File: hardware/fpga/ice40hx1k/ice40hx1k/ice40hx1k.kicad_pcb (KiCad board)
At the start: 2 copper layers, 58 parts, among them J1 Conn_01x20_Male, J2 Conn_01x20_Male, J3 Conn_01x20_Male, U1 LTC3406ES5, U5 AT25SF081-SSHD-X, U6 ICE40HX1K-VQ100(VQFP100), U7 AS7C34096A, X2 ASE-10MHz, X3 ASE-10MHz, X4 ASE-10MHz, X5 ASV-xxxMHz, X6 ASV-xxxMHz, X7 ASV-xxxMHz

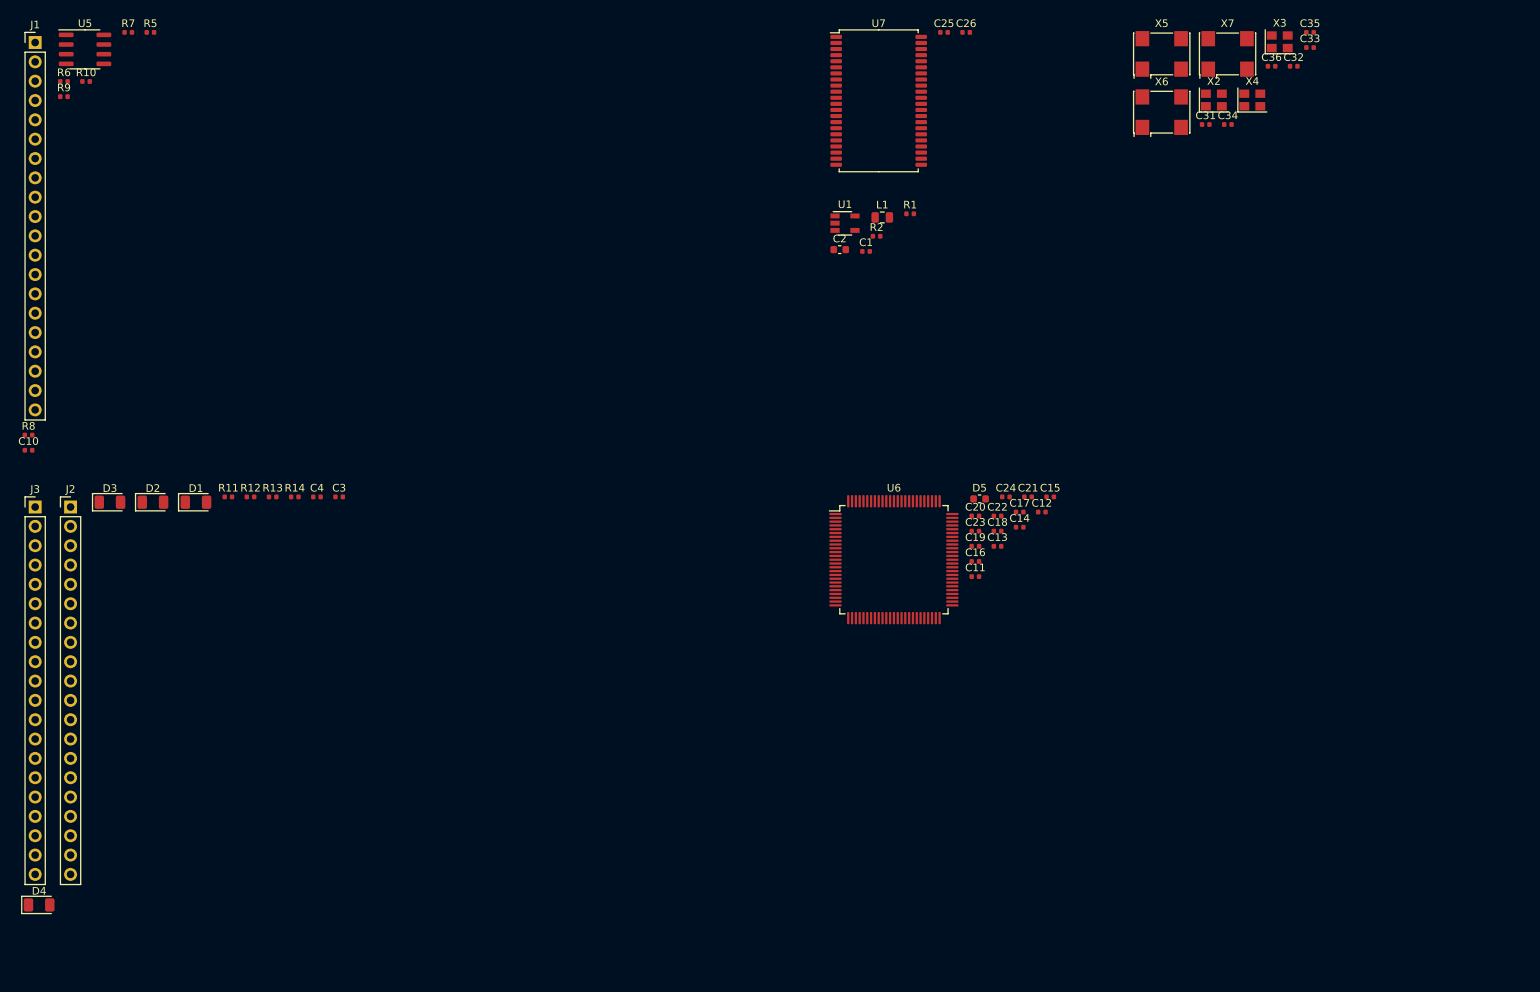
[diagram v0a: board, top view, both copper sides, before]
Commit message: std FPGA skeleton
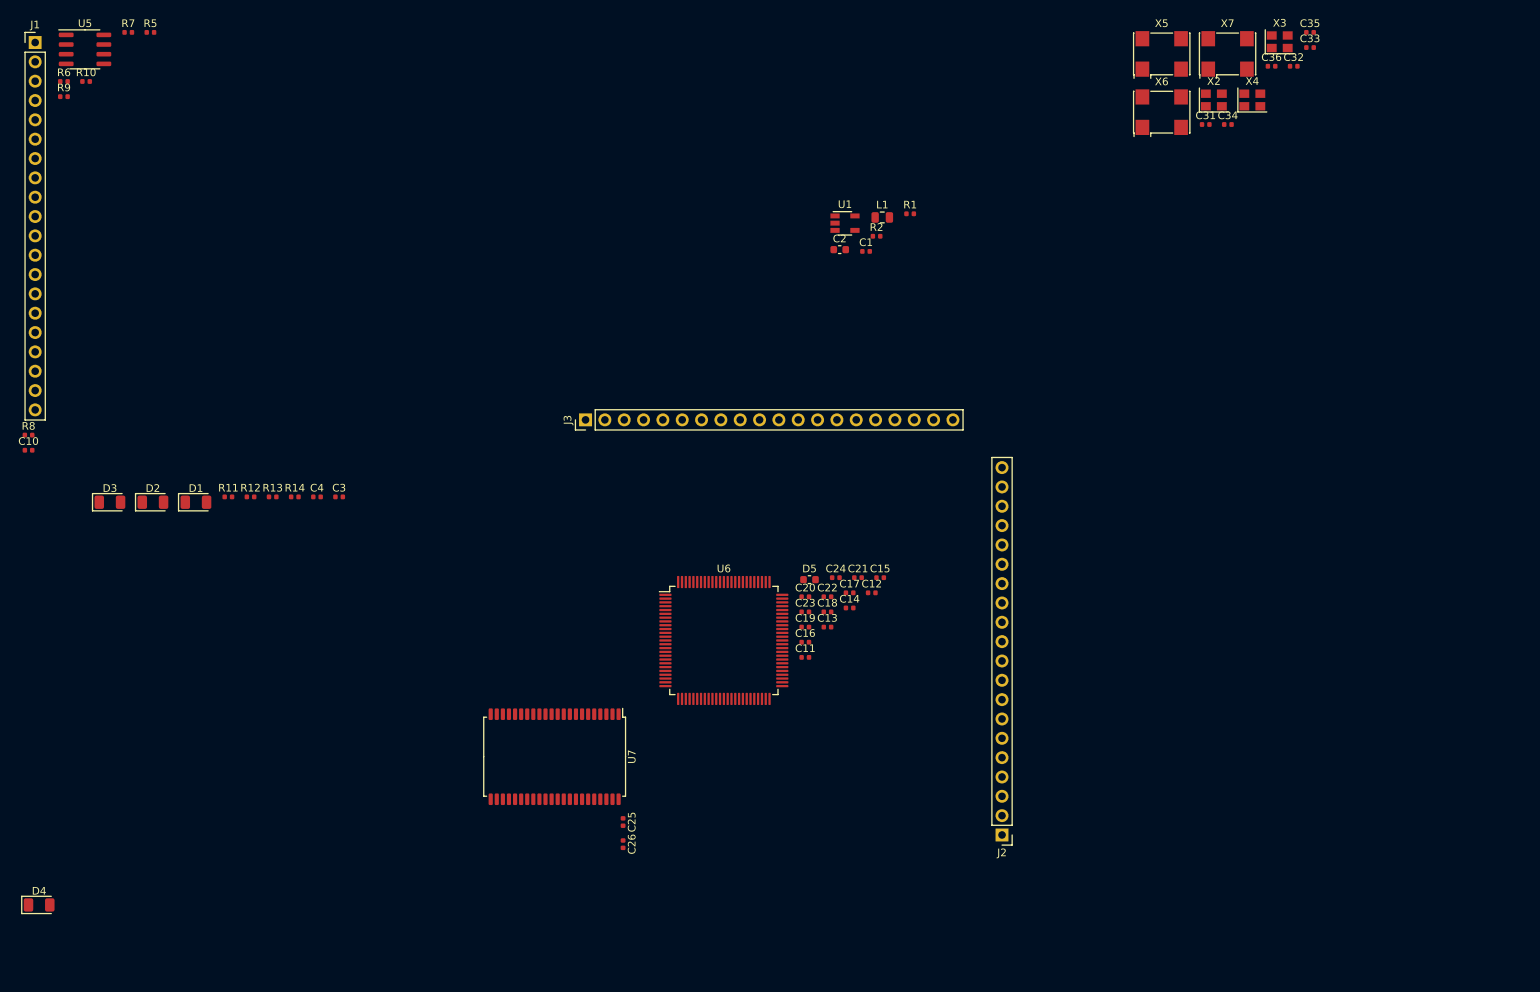
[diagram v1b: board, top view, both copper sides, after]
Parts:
- moved J2 129.7 mm to (191.9, 145.3), turned to 180 degrees
- moved C26 115.8 mm to (142.1, 146.5), turned to 270 degrees
- moved C25 112.0 mm to (142.1, 143.6), turned to 270 degrees
- moved U7 96.1 mm to (133.1, 135.0), turned to 270 degrees
- moved J3 73.2 mm to (137.2, 90.7), turned to 90 degrees
- moved C11 24.7 mm to (166.0, 121.9)
- moved C12 24.7 mm to (174.8, 113.5)
- moved C13 24.7 mm to (168.9, 118.0)
- moved C15 24.7 mm to (175.9, 111.5)
- moved C16 24.7 mm to (166.0, 120.0)
- moved C18 24.7 mm to (168.9, 116.0)
- moved C19 24.7 mm to (166.0, 118.0)
- moved C20 24.7 mm to (166.0, 114.0)
- moved C21 24.7 mm to (173.0, 111.5)
- moved C22 24.7 mm to (168.9, 114.0)
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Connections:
- J2 pad 12: IO100 -> IO78
- J2 pad 14: IO99 -> IO79
- J2 pad 16: IO97 -> IO80
- J2 pad 17: IO96 -> IO81
- J2 pad 18: IO95 -> IO82
- J2 pad 19: IO94 -> IO83
- J3 pad 11: IO85 -> IO93
- J3 pad 12: IO83 -> IO91
- J3 pad 14: IO82 -> IO90
- J3 pad 16: IO81 -> IO89
- J3 pad 17: IO80 -> IO87
- J3 pad 18: IO79 -> IO86
- J3 pad 19: IO78 -> IO85
- J3 pad 2: IO93 -> IO100
- J3 pad 3: IO91 -> IO99
- J3 pad 5: IO90 -> IO97
- J3 pad 6: IO89 -> IO96
- J3 pad 8: IO87 -> IO95
- J3 pad 9: IO86 -> IO94

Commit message: std FPGA skeleton
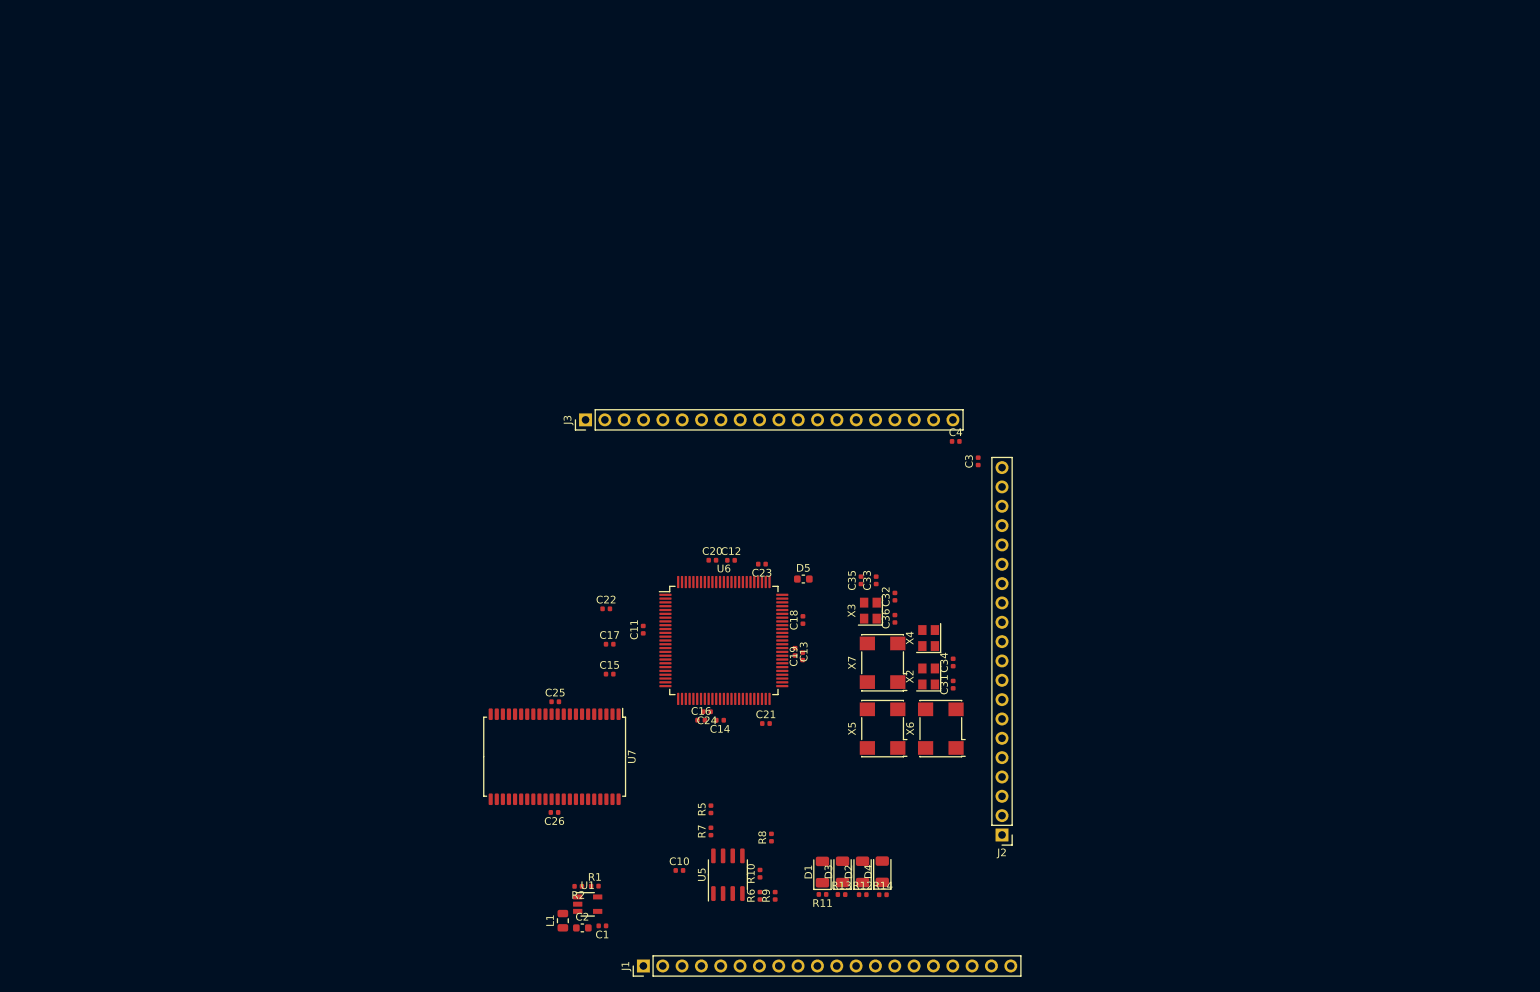
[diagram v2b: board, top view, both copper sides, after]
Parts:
- moved J1 145.3 mm to (144.8, 162.5), turned to 90 degrees
- moved R6 140.7 mm to (160.1, 153.3), turned to 90 degrees
- moved R9 140.5 mm to (162.1, 153.3), turned to 90 degrees
- moved U5 137.4 mm to (155.9, 150.5), turned to 90 degrees
- moved R10 136.6 mm to (160.1, 150.3), turned to 90 degrees
- moved R7 129.9 mm to (153.6, 144.8), turned to 90 degrees
- moved R5 125.8 mm to (153.6, 141.9), turned to 90 degrees
- moved R8 111.0 mm to (161.6, 145.6), turned to 90 degrees
- moved D4 110.8 mm to (176.2, 150.1), turned to 90 degrees
- moved D3 107.8 mm to (170.9, 150.1), turned to 90 degrees
- moved D2 105.1 mm to (173.6, 150.1), turned to 90 degrees
- moved C10 101.8 mm to (149.5, 149.9)
- moved L1 101.5 mm to (134.2, 156.5), turned to 90 degrees
- moved R1 97.6 mm to (138.4, 152.0)
- moved X5 95.9 mm to (176.2, 131.3), turned to 90 degrees
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
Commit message: std FPGA skeleton
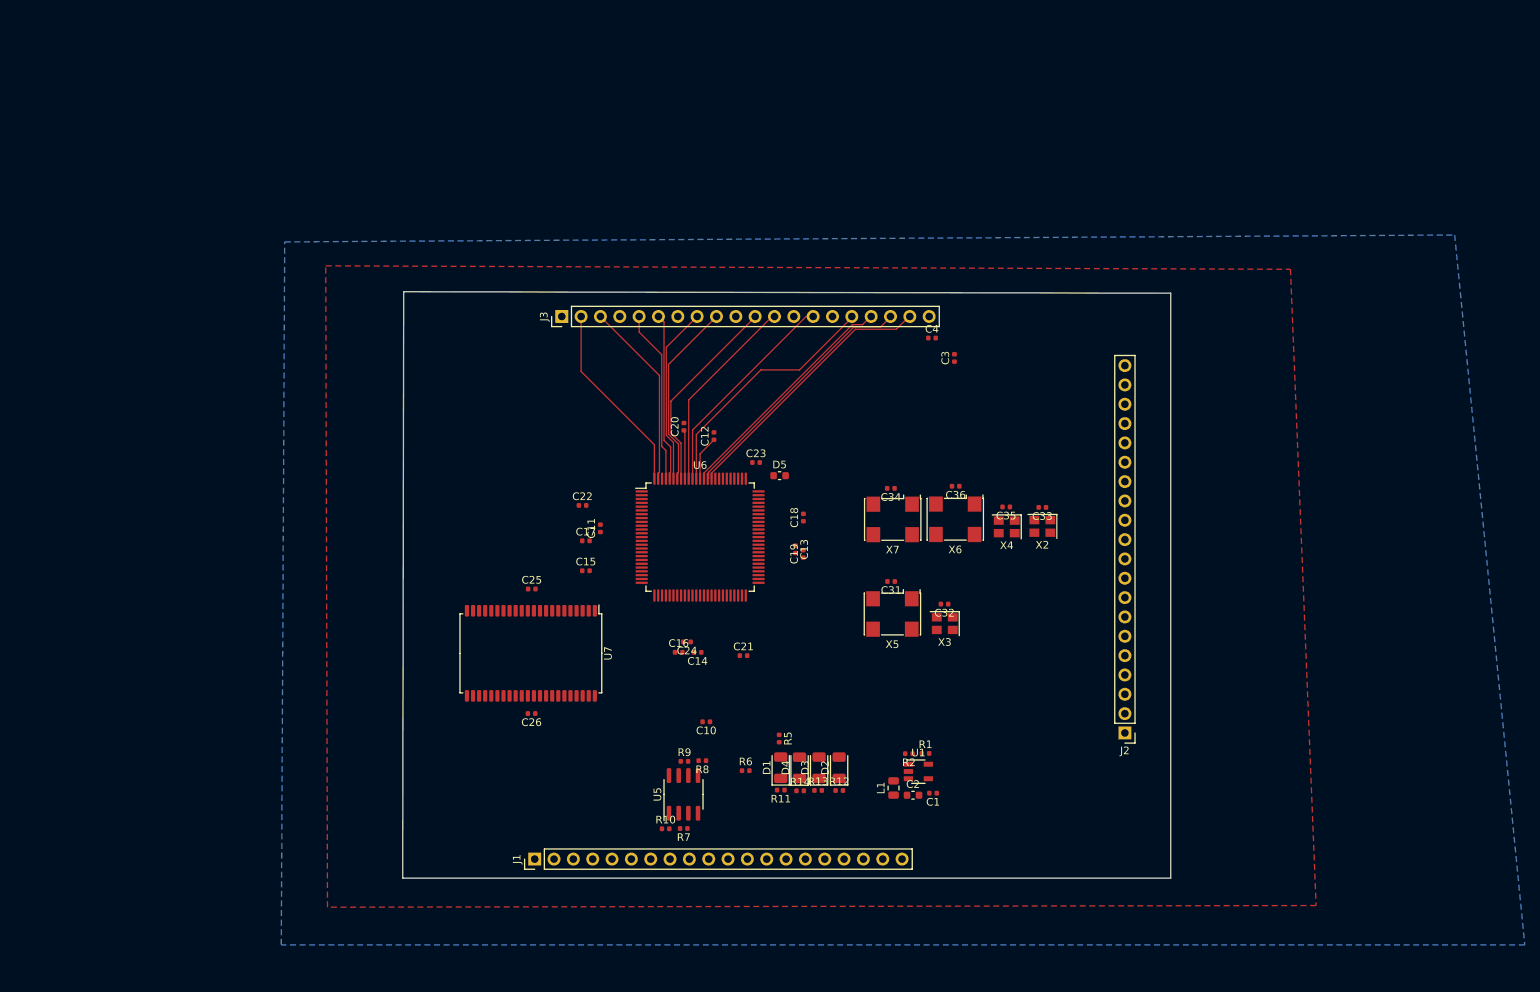
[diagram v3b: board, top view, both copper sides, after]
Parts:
- moved R1 46.8 mm to (181.8, 134.6)
- moved C1 46.8 mm to (182.8, 139.8)
- moved L1 46.8 mm to (177.6, 139.1)
- moved R2 46.8 mm to (179.7, 134.6)
- moved U1 46.8 mm to (180.9, 136.9)
- moved C2 46.8 mm to (180.2, 140.1)
- moved X6 27.6 mm to (185.7, 103.8), turned to 180 degrees
- moved X2 24.7 mm to (197.2, 104.7), turned to 180 degrees
- moved C34 24.3 mm to (177.3, 99.7), turned to 180 degrees
- moved C33 23.8 mm to (197.2, 102.2), turned to 180 degrees
- moved C35 21.4 mm to (192.4, 102.2), turned to 180 degrees
- moved R9 21.3 mm to (150.2, 135.6), turned to 0 degrees
- moved J2 21.0 mm to (208.0, 131.9)
- moved J1 20.0 mm to (130.5, 148.4)
- moved C10 19.8 mm to (153.0, 130.4), turned to 180 degrees
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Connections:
- J1 pad 10: SPI_CS -> SPI_IN
- J1 pad 11: SPI_IN -> SPI_SCK
- J1 pad 13: GND -> CRESET
- J1 pad 14: IO57 -> CDONE
- J1 pad 15: IO59 -> GND
- J1 pad 16: Net-(J1-Pad16) -> IO54
- J1 pad 17: GND -> IO56
- J1 pad 18: IO64 -> GND
- J1 pad 19: IO60 -> +3V3
- J1 pad 2: +3V3 -> Net-(J1-Pad2)
- J1 pad 3: GND -> Net-(J1-Pad3)
- J1 pad 4: IO56 -> GND
- J1 pad 5: IO54 -> Net-(J1-Pad5)
- J1 pad 6: GND -> Net-(J1-Pad6)
- J1 pad 7: CDONE -> Net-(J1-Pad7)
- J1 pad 8: CRESET -> GND
- J1 pad 9: SPI_SCK -> SPI_CS
- U6 pad 57: IO57 -> Net-(U6-Pad57)
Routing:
- net IO85: track 0.00 -> 35.2 mm
- net IO86: track 0.00 -> 33.4 mm
- net IO89: track 0.00 -> 32.6 mm
- net IO87: track 0.00 -> 31.0 mm
- net IO90: track 0.00 -> 28.7 mm
- net IO93: track 0.00 -> 26.3 mm
- net IO91: track 0.00 -> 25.8 mm
- net IO100: track 0.00 -> 25.5 mm
- net IO99: track 0.00 -> 25.1 mm
- net IO94: track 0.00 -> 24.8 mm
- net IO95: track 0.00 -> 23.2 mm
- net IO97: track 0.00 -> 22.8 mm
- net IO96: track 0.00 -> 22.3 mm
- net +3V3: track 0.00 -> 12.1 mm
- added copper zone on B.Cu, net GND
- added copper zone on F.Cu, net GND
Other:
- board outline added: 100.9 x 77 mm
- net class Default: clearance 0.2 -> 0.15; trace_width 0.25 -> 0.15; via_dia 0.8 -> 0.5; via_drill 0.4 -> 0.25
- rule trace_clearance: 0.2 -> 0.15
- rule trace_min: 0.2 -> 0.15
- rule via_min_drill: 0.3 -> 0.25
- rule via_min_size: 0.4 -> 0.5

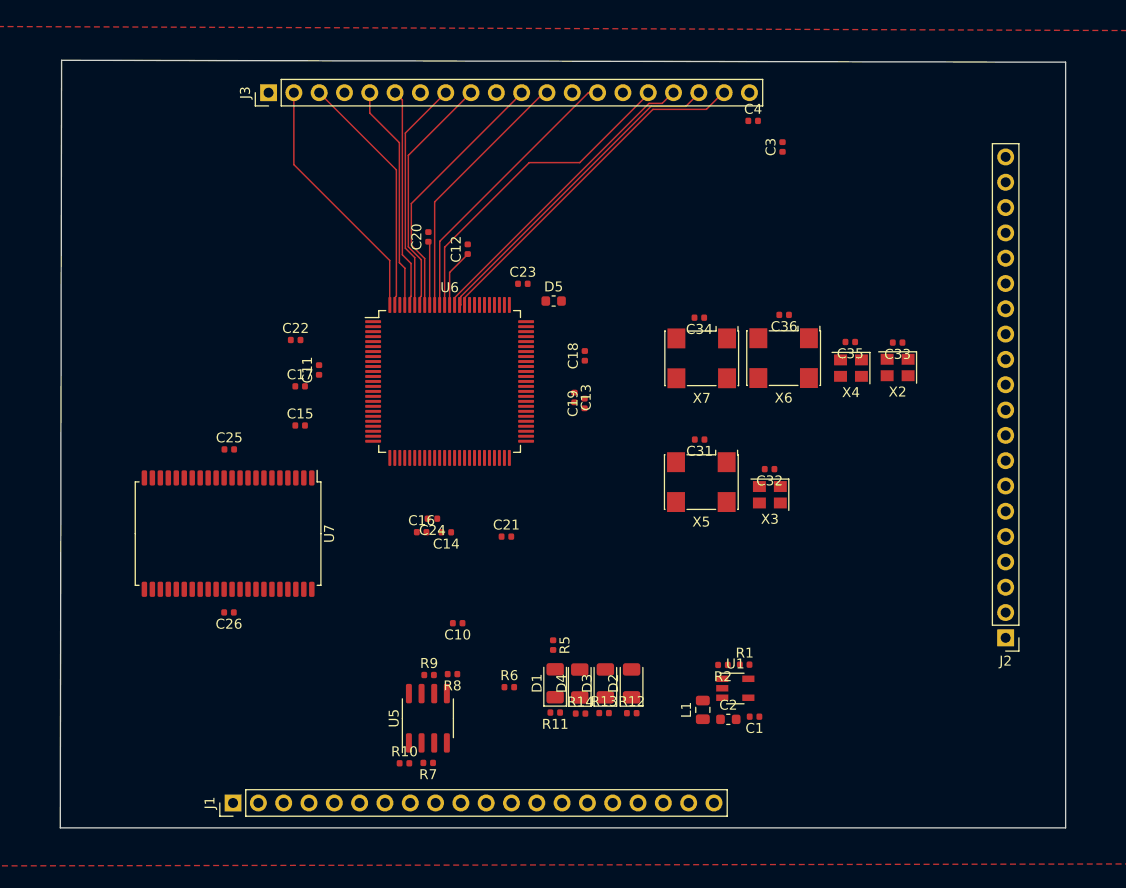
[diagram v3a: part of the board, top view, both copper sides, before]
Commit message: std FPGA skeleton
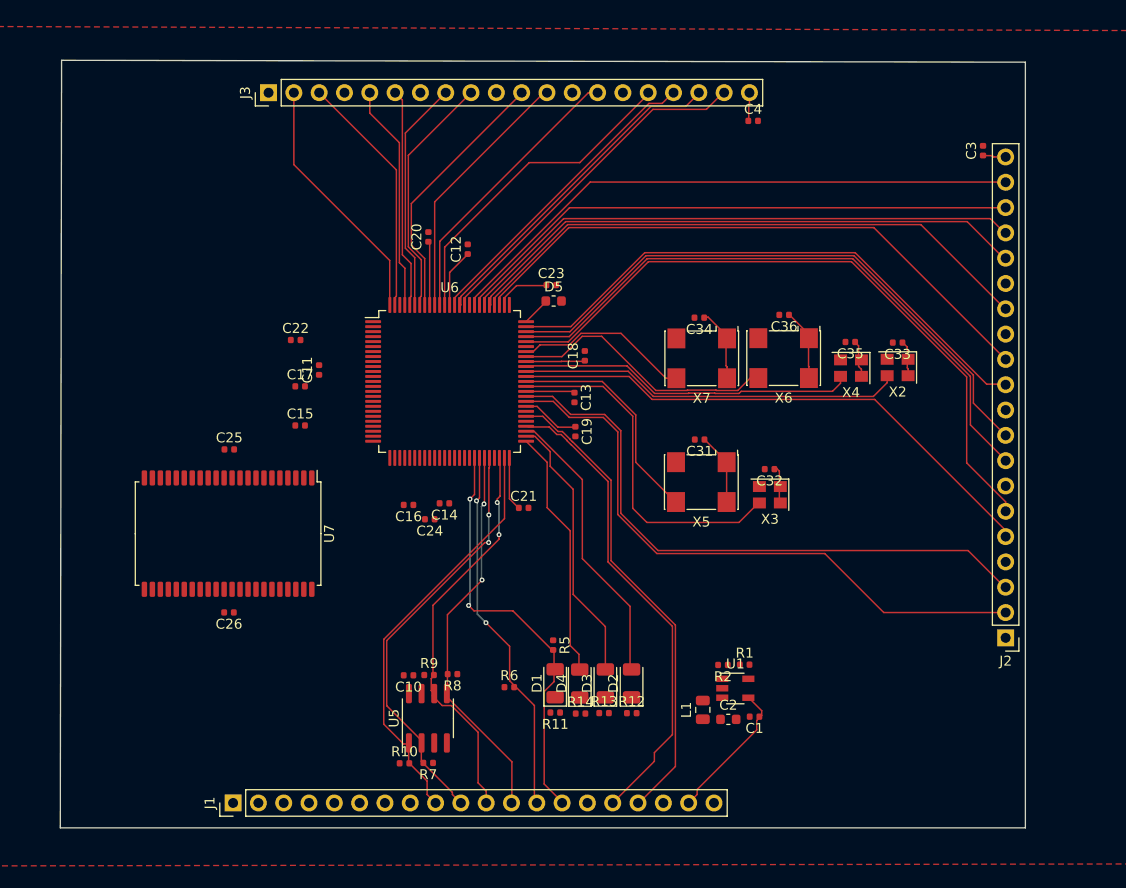
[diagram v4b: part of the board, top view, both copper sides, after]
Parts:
- moved C3 20.1 mm to (205.8, 83.0)
- moved C10 7.19 mm to (148.1, 135.6)
- moved C21 3.36 mm to (159.7, 118.8)
- moved C16 3.04 mm to (148.1, 118.5), turned to 180 degrees
- moved C19 2.96 mm to (164.8, 111.2), turned to 270 degrees
- moved C14 2.92 mm to (151.7, 118.4)
- moved C23 2.85 mm to (162.4, 96.5)
- moved C24 0.27 mm to (150.2, 120.0)
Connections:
- J2 pad 11: IO73 -> IO74
- J2 pad 2: IO60 -> IO59
- J2 pad 3: IO59 -> IO60
- J2 pad 9: IO74 -> IO73
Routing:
- net +3V3: track 12.1 -> 81.1 mm
- net IO71: track 0.00 -> 67.6 mm
- net IO72: track 0.00 -> 62.7 mm
- net IO59: track 0.00 -> 61.6 mm
- net IO60: track 0.00 -> 61.0 mm
- net IO73: track 0.00 -> 60.2 mm
- net IO78: track 0.00 -> 60.2 mm
- net IO83: track 0.00 -> 58.7 mm
- net IO79: track 0.00 -> 58.6 mm
- net IO80: track 0.00 -> 57.4 mm
- net IO82: track 0.00 -> 57.2 mm
- net IO81: track 0.00 -> 57.0 mm
- net IO74: track 0.00 -> 56.8 mm
- net IO64: track 0.00 -> 55.4 mm
- net IO56: track 0.00 -> 48.0 mm
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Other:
- board size 100.9 x 77 mm -> 96.8 x 77 mm
